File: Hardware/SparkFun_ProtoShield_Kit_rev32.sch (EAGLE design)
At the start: 29 parts

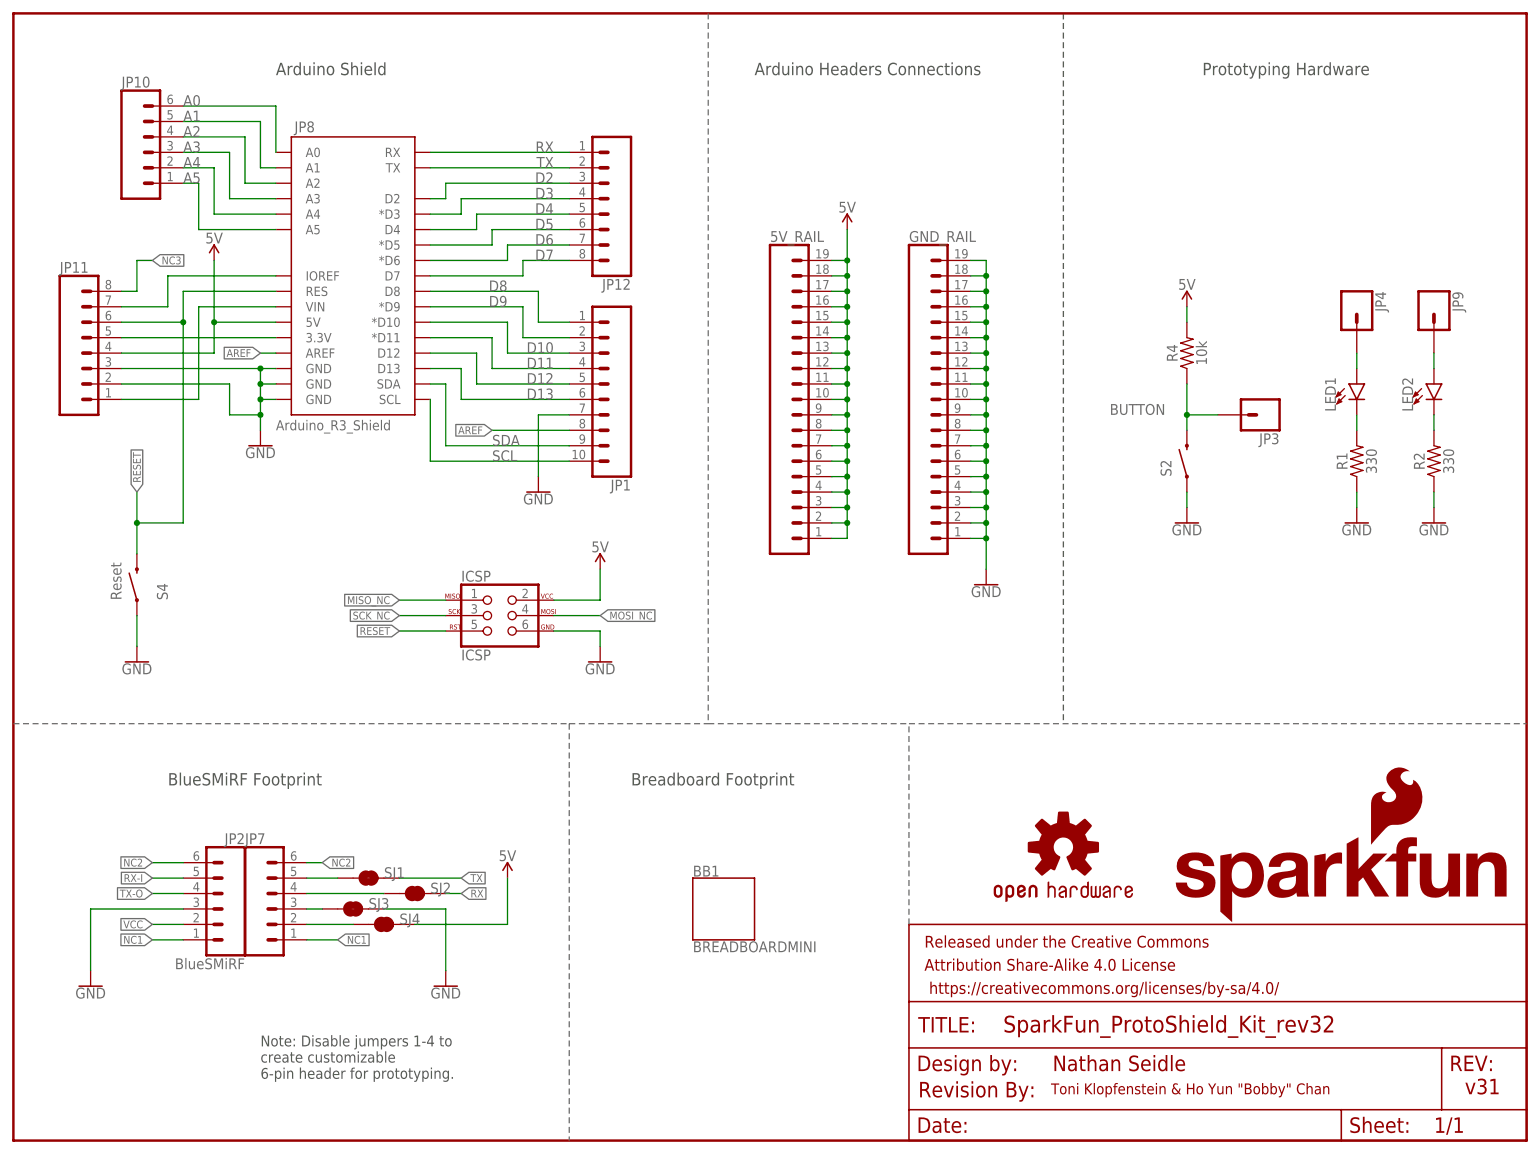
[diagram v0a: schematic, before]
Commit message: Update_Proto2
-Shifted the mini-breadboard footprint
-Moved Vcc and GND rails to bottom for access
-Added VDD as an option
-Added Disconnected Breadboard rails based on Jim’s Design (GPS Shield), best of both worlds
-Add 2x more through hole pins for prototyping area
-Shifted Prototyping Hardware Around
-Switch Hardware Serial to Software -Serial to prevent bricking UART device
-Added Vcc and GND traces through mouse bite just in case
-Adjusted Header D8-SCL  so that the shield can stack with a breadboard (Michelle’s Suggestion)
-Added little bit more silkscreen to distinguish location of stackable headers
-Moved Reset button up for better access
-Switched Momentary Push Button Package to Double PTH
-Update Schematic
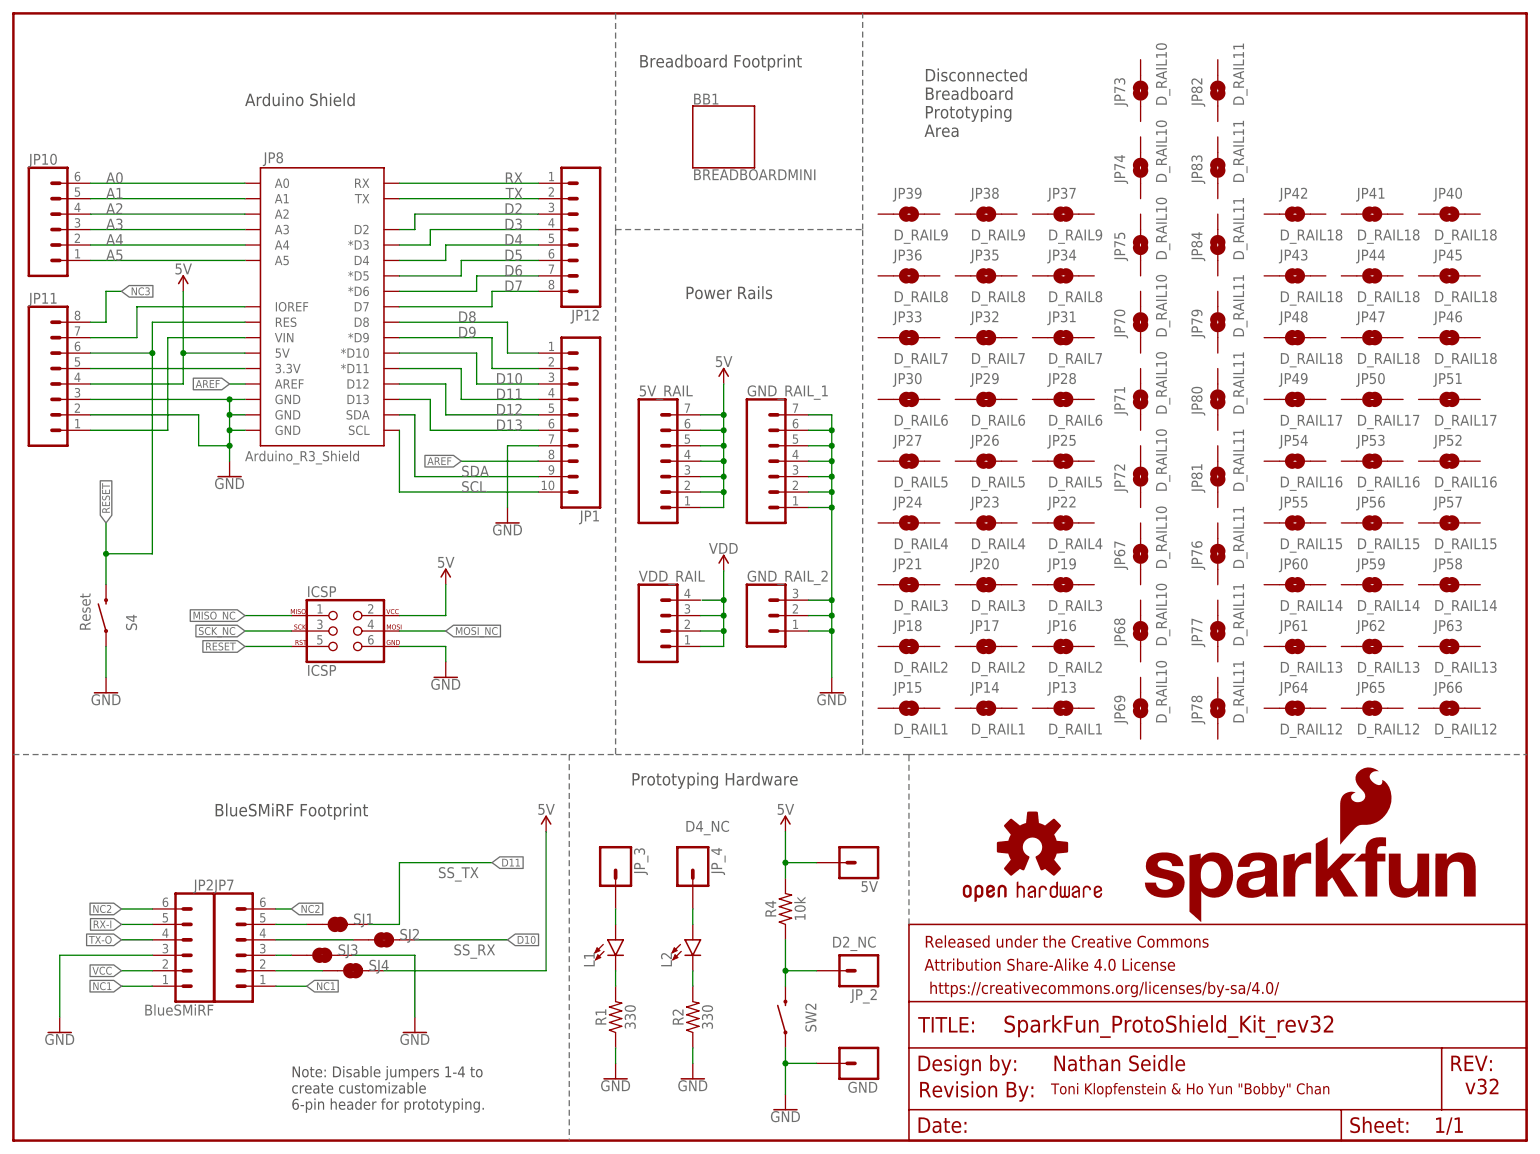
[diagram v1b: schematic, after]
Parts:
- removed GND_RAIL: (no value), SparkFun-Connectors:CONN_19
- removed JP3, JP4, JP9: (no value), SparkFun-Connectors:CONN_01
- removed LED1, LED2: (no value), SparkFun-LED:LED3MM
- removed S2: MOMENTARY-SWITCH-SPST-PTH-6.0MM-KIT, SparkFun-Switches:MOMENTARY-SWITCH-SPST-PTH-6.0MM-KIT
- added 5V, GND, JP_2, JP_3, JP_4: (no value), SparkFun-Connectors:CONN_01
- added GND_RAIL_1: (no value), SparkFun-Connectors:CONN_07NO_SILK
- added GND_RAIL_2: (no value), SparkFun-Connectors:CONN_031X03_NO_SILK
- added JP13, JP14, JP15: D_RAIL1, SparkFun-Jumpers:JUMPER-SMT_2_NO_NO-SILK
- added JP16, JP17, JP18: D_RAIL2, SparkFun-Jumpers:JUMPER-SMT_2_NO_NO-SILK
- added JP19, JP20, JP21: D_RAIL3, SparkFun-Jumpers:JUMPER-SMT_2_NO_NO-SILK
- added JP22, JP23, JP24: D_RAIL4, SparkFun-Jumpers:JUMPER-SMT_2_NO_NO-SILK
- added JP25, JP26, JP27: D_RAIL5, SparkFun-Jumpers:JUMPER-SMT_2_NO_NO-SILK
- added JP28, JP29, JP30: D_RAIL6, SparkFun-Jumpers:JUMPER-SMT_2_NO_NO-SILK
- added JP31, JP32, JP33: D_RAIL7, SparkFun-Jumpers:JUMPER-SMT_2_NO_NO-SILK
- added JP34, JP35, JP36: D_RAIL8, SparkFun-Jumpers:JUMPER-SMT_2_NO_NO-SILK
- added JP37, JP38, JP39: D_RAIL9, SparkFun-Jumpers:JUMPER-SMT_2_NO_NO-SILK
- added JP40, JP41, JP42, JP43, JP44, JP45, JP46, JP47, JP48: D_RAIL18, SparkFun-Jumpers:JUMPER-SMT_2_NO_NO-SILK
- added JP49, JP50, JP51: D_RAIL17, SparkFun-Jumpers:JUMPER-SMT_2_NO_NO-SILK
- added JP52, JP53, JP54: D_RAIL16, SparkFun-Jumpers:JUMPER-SMT_2_NO_NO-SILK
- added JP55, JP56, JP57: D_RAIL15, SparkFun-Jumpers:JUMPER-SMT_2_NO_NO-SILK
- added JP58, JP59, JP60: D_RAIL14, SparkFun-Jumpers:JUMPER-SMT_2_NO_NO-SILK
- added JP61, JP62, JP63: D_RAIL13, SparkFun-Jumpers:JUMPER-SMT_2_NO_NO-SILK
- added JP64, JP65, JP66: D_RAIL12, SparkFun-Jumpers:JUMPER-SMT_2_NO_NO-SILK
- added JP67, JP68, JP69, JP70, JP71, JP72, JP73, JP74, JP75: D_RAIL10, SparkFun-Jumpers:JUMPER-SMT_2_NO_NO-SILK
- added JP76, JP77, JP78, JP79, JP80, JP81, JP82, JP83, JP84: D_RAIL11, SparkFun-Jumpers:JUMPER-SMT_2_NO_NO-SILK
- added L1, L2: (no value), SparkFun-LED:LED3MM
- added SW2: MOMENTARY-SWITCH-SPST-PTH-6.0MM, SparkFun-Switches:MOMENTARY-SWITCH-SPST-PTH-6.0MM
- added VDD_RAIL: (no value), SparkFun-Connectors:CONN_041X04_NO_SILK
- 5V_RAIL: device SparkFun-Connectors:CONN_19 -> SparkFun-Connectors:CONN_07NO_SILK
- S4: value MOMENTARY-SWITCH-SPST-PTH-6.0MM-KIT -> MOMENTARY-SWITCH-SPST-PTH-6.0MM; device SparkFun-Switches:MOMENTARY-SWITCH-SPST-PTH-6.0MM-KIT -> SparkFun-Switches:MOMENTARY-SWITCH-SPST-PTH-6.0MM
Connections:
- net A0 renamed N$2
- net A3 renamed N$4
- net A4 renamed N$3
- removed net BUTTON: JP3.1, R4.1, S2.2
- removed net LED1: JP4.1, LED1.A
- removed net LED2: JP9.1, LED2.A
- new net D2_NC: JP_2.1, R4.1, SW2.2
- new net JP3: JP_3.1, L1.A
- new net JP4: JP_4.1, L2.A
- new net VDD: VDD_RAIL.1, VDD_RAIL.2, VDD_RAIL.3
- net 5V: now also 5V.1; no longer 5V_RAIL.10, 5V_RAIL.11, 5V_RAIL.12, 5V_RAIL.13, 5V_RAIL.14, 5V_RAIL.15, 5V_RAIL.16, 5V_RAIL.17, 5V_RAIL.18, 5V_RAIL.19, 5V_RAIL.8, 5V_RAIL.9
- net D10: now also SJ2.2
- net D11: now also SJ1.2
- net GND: now also GND.1, GND_RAIL_1.1, GND_RAIL_1.2, GND_RAIL_1.3, GND_RAIL_1.4, GND_RAIL_1.5, GND_RAIL_1.6, GND_RAIL_1.7, GND_RAIL_2.1, GND_RAIL_2.2, GND_RAIL_2.3, SW2.1; no longer GND_RAIL.1, GND_RAIL.10, GND_RAIL.11, GND_RAIL.12, GND_RAIL.13, GND_RAIL.14, GND_RAIL.15, GND_RAIL.16, GND_RAIL.17, GND_RAIL.18, GND_RAIL.19, GND_RAIL.2, GND_RAIL.3, GND_RAIL.4, GND_RAIL.5, GND_RAIL.6, GND_RAIL.7, GND_RAIL.8, GND_RAIL.9, S2.1
- net N$6: now also L1.C; no longer LED1.C
- net N$7: now also L2.C; no longer LED2.C
- net RX: no longer SJ2.2
- net TX: no longer SJ1.2
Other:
- note added: "D3_NC"
- note added: "D4_NC"
- note added: "Disconnected Breadboard Prototyping Area"
- note added: "Power Rails"
- note added: "SS_RX"
- note added: "SS_TX"
- note added: "v32"
- note removed: "Arduino Headers Connections"
- note removed: "v31"
- moved on the sheet: BB1, ICSP, JP1, JP10, JP11, JP12, JP2, JP7, JP8, R1, R2, R4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

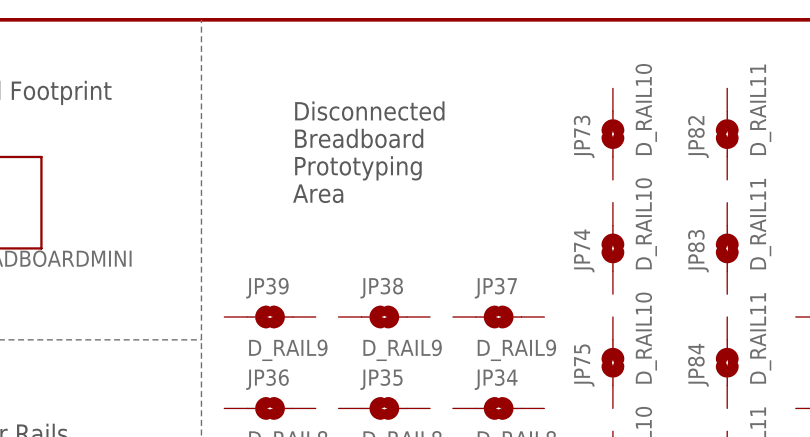
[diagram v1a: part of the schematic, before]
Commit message: Proto 2 QC Update
-Adjust normally open (NO) jumper pad rails so the silkscreen is not over the vias to prevent errors.
-Adjust the "+" 5V trace intersection for the prototyping hardware.
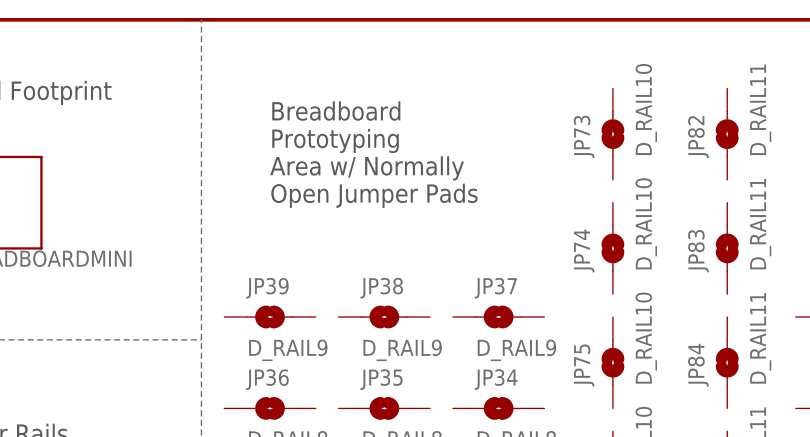
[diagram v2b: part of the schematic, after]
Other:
- note added: "Breadboard Prototyping Area w/ Normally Open Jumper Pads"
- note removed: "Disconnected Breadboard Prototyping Area"
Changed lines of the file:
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@@
 <wire x1="147.32" y1="63.5" x2="248.92" y2="63.5" width="0.1524" layer="95" style="shortdash"/>
 <wire x1="147.32" y1="35.56" x2="147.32" y2="63.5" width="0.1524" layer="95" style="shortdash"/>
-<text x="149.86" y="165.1" size="2.032" layer="97" font="vector" ratio="15">Disconnected
-Breadboard
+<text x="147.32" y="165.1" size="2.032" layer="97" font="vector" ratio="15">Breadboard
 Prototyping
-Area</text>
+Area w/ Normally
+Open Jumper Pads</text>
 <wire x1="139.7" y1="63.5" x2="139.7" y2="149.86" width="0.1524" layer="95" style="shortdash"/>
 <wire x1="139.7" y1="149.86" x2="139.7" y2="185.42" width="0.1524" layer="95" style="shortdash"/>

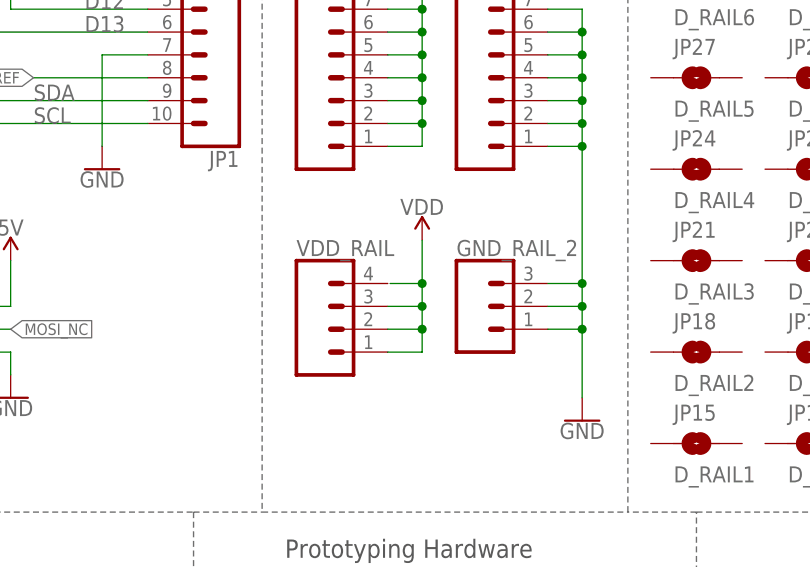
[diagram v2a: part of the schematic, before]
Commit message: Airwires
-Fix airwires on analog pins, 5V rail, and VDD rail.
-Fix tiny floating net wire in schematic.
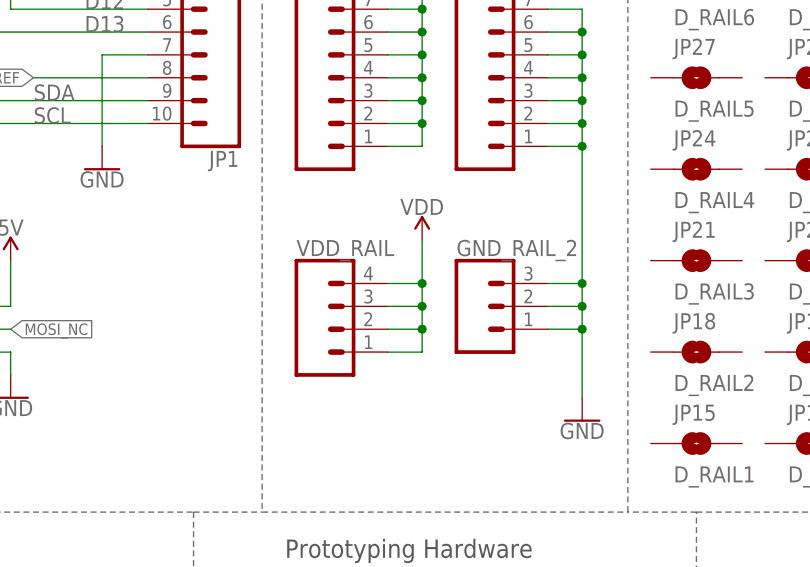
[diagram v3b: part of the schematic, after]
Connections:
- net VDD: now also VDD_RAIL.4
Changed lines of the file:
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@@
 <setting verticaltext="up"/>
 </settings>
-<grid distance="0.1" unitdist="inch" unit="inch" style="lines" multiple="1" display="no" altdistance="0.01" altunitdist="inch" altunit="inch"/>
+<grid distance="0.01" unitdist="inch" unit="inch" style="lines" multiple="1" display="no" altdistance="0.01" altunitdist="inch" altunit="inch"/>
 <layers>
 <layer number="1" name="Top" color="4" fill="1" visible="no" active="no"/>
@@
 <junction x="116.84" y="83.82"/>
 <pinref part="VDD" gate="G$1" pin="VCC_2"/>
-<wire x1="113.284" y1="88.9" x2="116.84" y2="88.9" width="0.1524" layer="91"/>
+<pinref part="VDD_RAIL" gate="G$1" pin="4"/>
+<wire x1="113.03" y1="88.9" x2="116.84" y2="88.9" width="0.1524" layer="91"/>
 <junction x="116.84" y="88.9"/>
 </segment>
